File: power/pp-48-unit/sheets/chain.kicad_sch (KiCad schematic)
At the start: 2 parts, among them J301 CHAIN IN, J302 CHAIN OUT

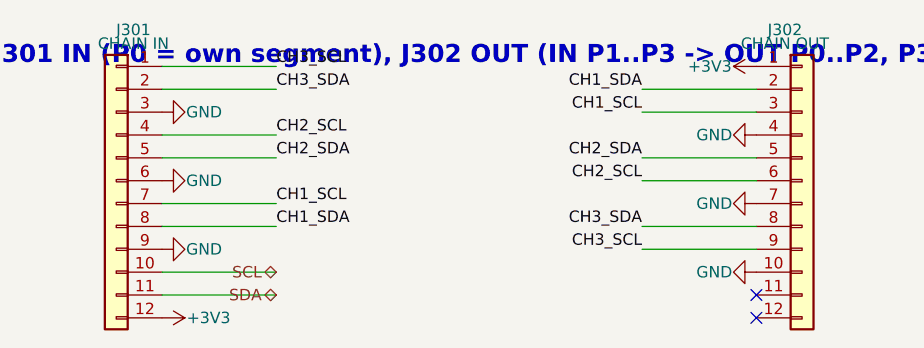
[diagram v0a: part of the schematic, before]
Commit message: pp-48 chained plane: unit board 76 x 72 (9 mm left margin for chain IN J301 + holes, user; slots as rev1 at x 100 / 125; 17 mm input strip with XT60, unit hot-swap, chain OUT J302) and core board 56 x 72 (rev1 core minus the tile, 8 mm right margin for chain OUT J301 + holes, mux U6 by the header, XT30 at the bottom) placed as drafts by tools/place_unit.py / place_core.py (boardfit.py helpers); chain headers on B, pins at v 39..61 on every board; pinout swapped so IN pin 1 = 3V3 / P0 at the bottom on B (flat cable n -> 13 - n); DRC 0 errors besides unconnected, parity clean; not routed; handoff
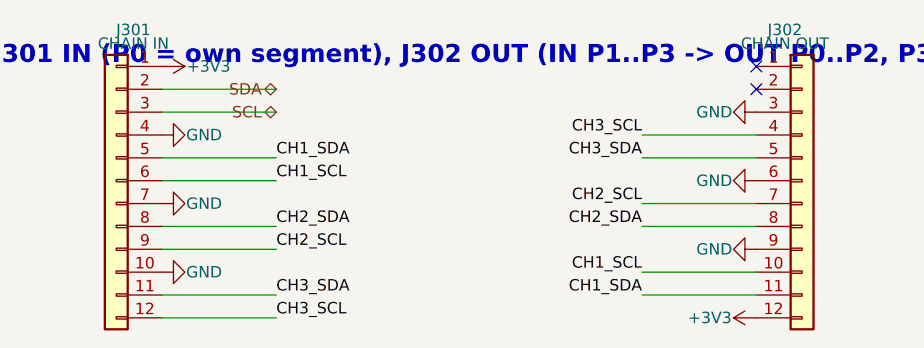
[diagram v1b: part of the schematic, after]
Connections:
- net +3V3: now also J301.1 (Pin_1), J302.12 (Pin_12); no longer J301.12 (Pin_12), J302.1 (Pin_1)
- net CH1_SCL: now also J301.6 (Pin_6), J302.10 (Pin_10); no longer J301.7 (Pin_7), J302.3 (Pin_3)
- net CH1_SDA: now also J301.5 (Pin_5), J302.11 (Pin_11); no longer J301.8 (Pin_8), J302.2 (Pin_2)
- net CH2_SCL: now also J301.9 (Pin_9), J302.7 (Pin_7); no longer J301.4 (Pin_4), J302.6 (Pin_6)
- net CH2_SDA: now also J301.8 (Pin_8), J302.8 (Pin_8); no longer J301.5 (Pin_5), J302.5 (Pin_5)
- net CH3_SCL: now also J301.12 (Pin_12), J302.4 (Pin_4); no longer J301.1 (Pin_1), J302.9 (Pin_9)
- net CH3_SDA: now also J301.11 (Pin_11), J302.5 (Pin_5); no longer J301.2 (Pin_2), J302.8 (Pin_8)
- net GND: now also J301.10 (Pin_10), J301.4 (Pin_4), J301.7 (Pin_7), J302.3 (Pin_3), J302.6 (Pin_6), J302.9 (Pin_9); no longer J301.3 (Pin_3), J301.6 (Pin_6), J301.9 (Pin_9), J302.10 (Pin_10), J302.4 (Pin_4), J302.7 (Pin_7)
- net SCL: now also J301.3 (Pin_3); no longer J301.10 (Pin_10)
- net SDA: now also J301.2 (Pin_2); no longer J301.11 (Pin_11)

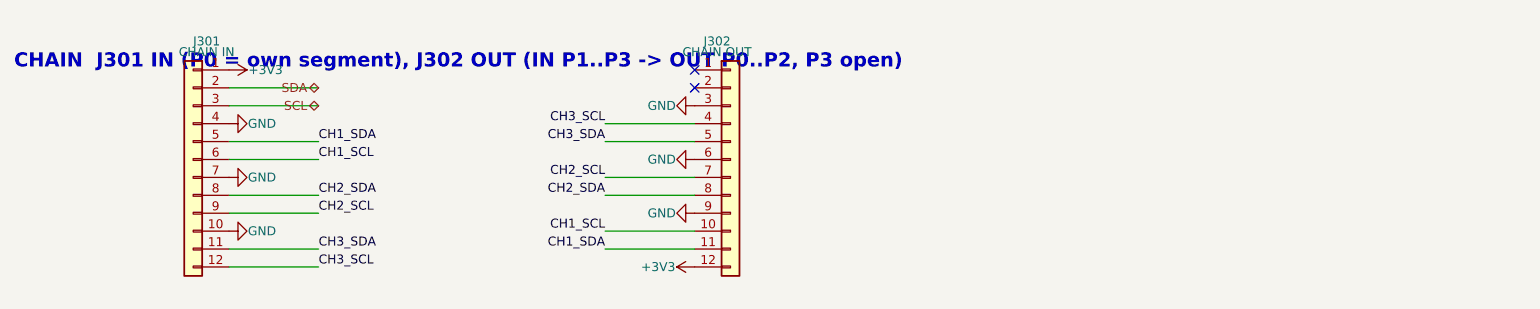
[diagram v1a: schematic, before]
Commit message: pp-48 plane boards: press deadline line (docs/press-deadline-line.md decided: option B + A) on a 14-pin chain (S14B-PH-K-S C157938; 13 PRESS_EN, 14 EXP_RSTN, cable n -> 15 - n, pins v 35..61); unit Q10 / R31 switch the photoMOS LED returns (PRESS_RTN), core U301 74LVC1G123 deadline (pp:74LVC1G123 single-unit copy) on PC6 PRESS_TRIG, PC7 EXP_RSTN to the units' /RESET; ERC 0 both; boards rebuilt and placed, unit 78.5 x 72 with the strip power path re-placed top-down; unit routing tools (route_unit.py hand copper + In2 band / +3V3 trunk, unitsplit.py, route_unit.sh flow): DRC 0 errors, ~10 unconnected at expander U5; core placed, not routed; pmmount.py restored from granite_controller; ADR 0005 decision 4; handoff
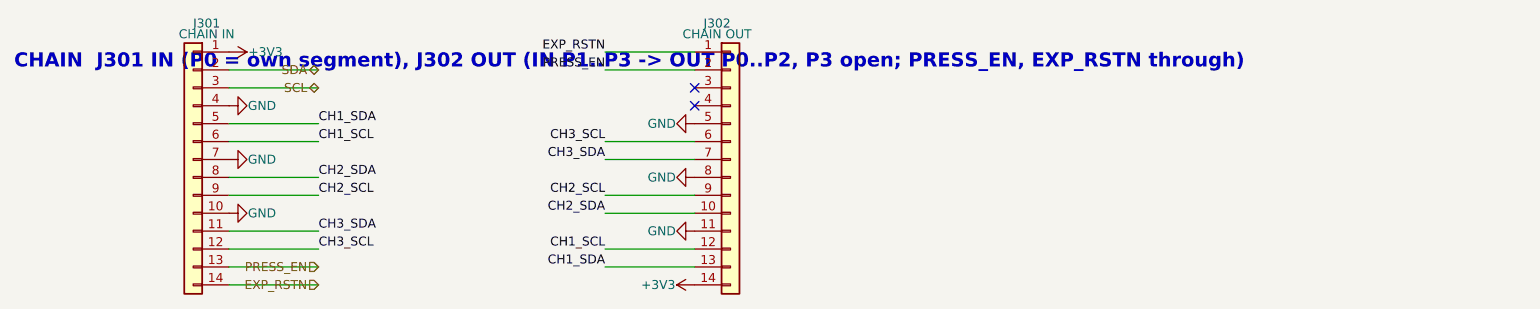
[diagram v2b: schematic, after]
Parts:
- J301, J302: footprint Connector_JST:JST_PH_S12B-PH-K_1x12_P2.00mm_Horizontal -> Connector_JST:JST_PH_S14B-PH-K_1x14_P2.00mm_Horizontal; symbol Connector_Generic:Conn_01x12 -> Connector_Generic:Conn_01x14; LCSC C157943 -> C157938; MPN JST S12B-PH-K-S(LF)(SN) -> JST S14B-PH-K-S(LF)(SN)
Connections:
- net +3V3: now also J302.14 (Pin_14); no longer J302.12 (Pin_12)
- net CH1_SCL: now also J302.12 (Pin_12); no longer J302.10 (Pin_10)
- net CH1_SDA: now also J302.13 (Pin_13); no longer J302.11 (Pin_11)
- net CH2_SCL: now also J302.9 (Pin_9); no longer J302.7 (Pin_7)
- net CH2_SDA: now also J302.10 (Pin_10); no longer J302.8 (Pin_8)
- net CH3_SCL: now also J302.6 (Pin_6); no longer J302.4 (Pin_4)
- net CH3_SDA: now also J302.7 (Pin_7); no longer J302.5 (Pin_5)
- net GND: now also J302.11 (Pin_11), J302.5 (Pin_5), J302.8 (Pin_8); no longer J302.3 (Pin_3), J302.6 (Pin_6), J302.9 (Pin_9)
- net EXP_RSTN: now reaches J302.1 (Pin_1)
- net EXP_RSTN: now also J301.14 (Pin_14)
- net PRESS_EN: now reaches J302.2 (Pin_2)
- net PRESS_EN: now also J301.13 (Pin_13)
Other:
- note added: "CHAIN J301 IN (P0 = own segment), J302 OUT (IN P1..P3 -> OUT P0..P2, P3 open; PRESS_EN, EXP_RSTN through)"
- note removed: "CHAIN J301 IN (P0 = own segment), J302 OUT (IN P1..P3 -> OUT P0..P2, P3 open)"
